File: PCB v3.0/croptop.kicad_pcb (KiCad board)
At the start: 4 copper layers, 190.1 x 122.2 mm, 273 parts, among them J1 TSM-106-01-L-SV, J10 1702474, J11 1702474, J12 1702474, J13 1702474, J14 1702474, J15 TSM-112-01-L-DV, J16 DM3D-SF, J17 Conn_01x01, J18 Conn_01x01, J2 0473460001, J3 87583-2010BLF, J4 NREC004SABC-M30RC, J5 Conn_01x01, J6 Conn_01x01, J7 1702474, J8 1702474, J9 1702474, Q1 BSS138, Q2 BSS84, Q3 Q2319ADS-T1-GE3, Q4 BSS138, Q5 BSS138, Q6 BSS138, SW1 SW_Push, SW2 SW_Push, SW3 SW_Push, SW4 SW_Push, U1 PIC32MX795F512L, U18 74HCT125D653, U19 AP22802AW5, U2 REG71055DDC, U20 AD7799, U21 AP22802AW5, U22 TPD4E1U06DBV, U23 AP22802AW5, U24 TPD4E1U06DBV, U25 TPD4E1U06DBV, U26 TPD4E1U06DBV, U27 DRV8872, U28 DRV8825, U29 AP22802AW5, U3 AP22802AW5, U30 TPD4E1U06DBV, U31 TPD4E1U06DBV, U32 AP22802AW5, U33 AP22802AW5, U34 TPD4E1U06DBV, U35 TPD4E1U06DBV, U36 AP22802AW5, U37 TPD4E1U06DBV, U38 TPD4E1U06DBV, U39 LIS3DSHTR, U40 CAM-M8C-0, U41 Si7006-A20, U5 TPS62131RGT, U6 TPS70950DBV, U7 TPD4E1U06DBV, U8 TPD4E1U06DBV, Y1 ABLS-8.000MHZ-B4-T, Y3 ABS07-32.768KHZ-1-T

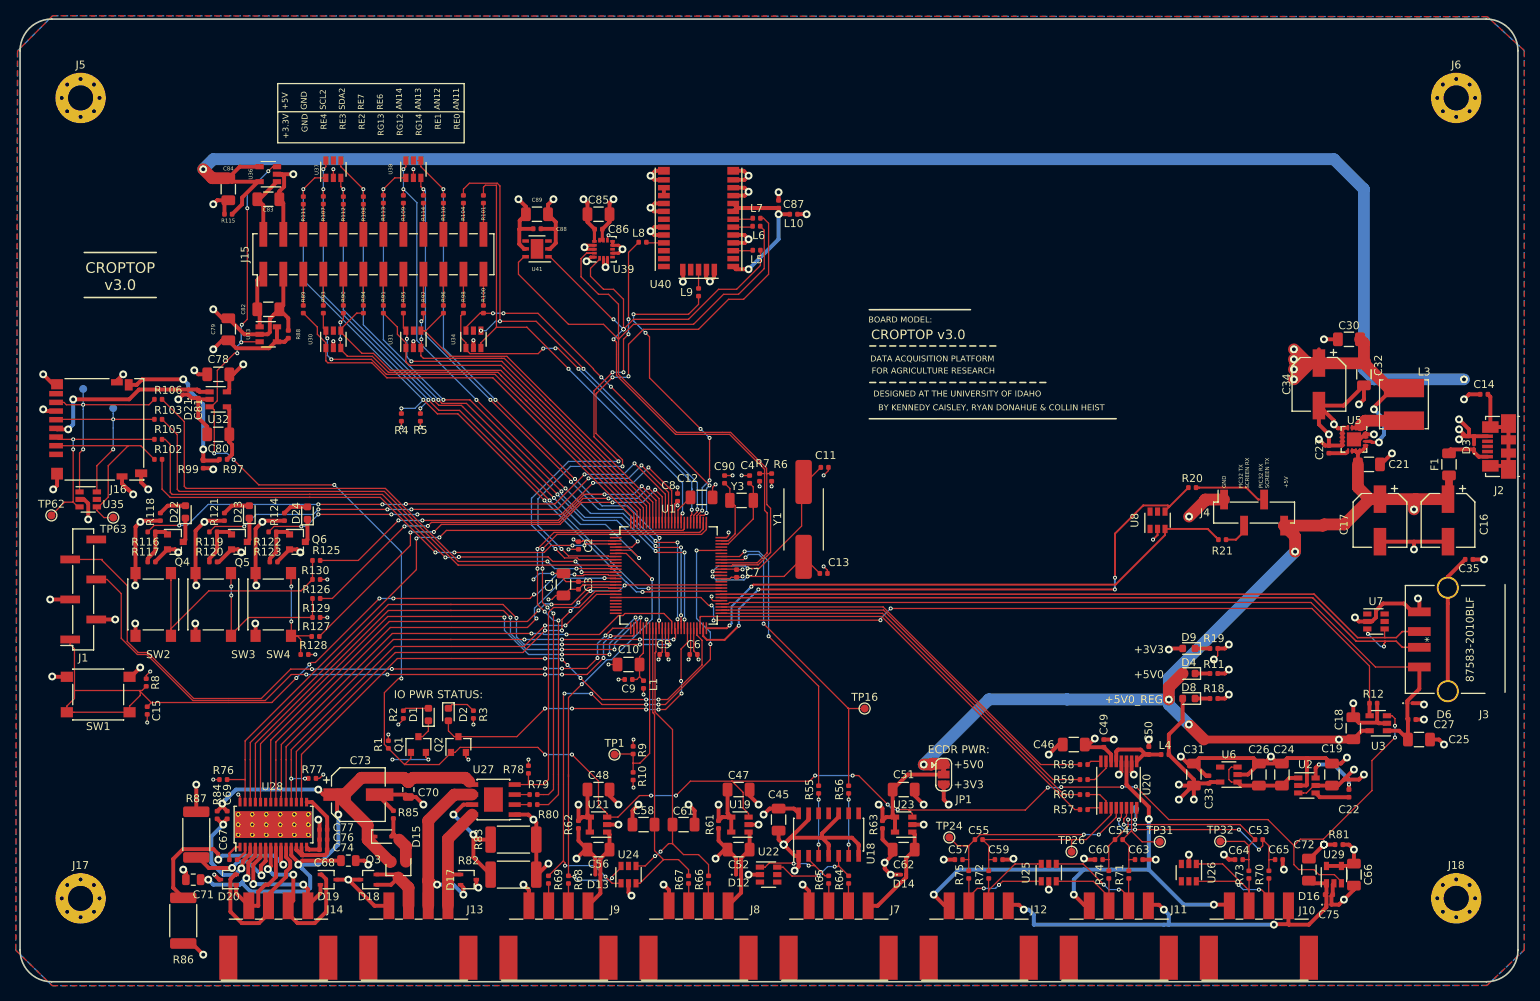
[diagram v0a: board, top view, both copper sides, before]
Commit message: Updated readme, added graphics to PCBv3
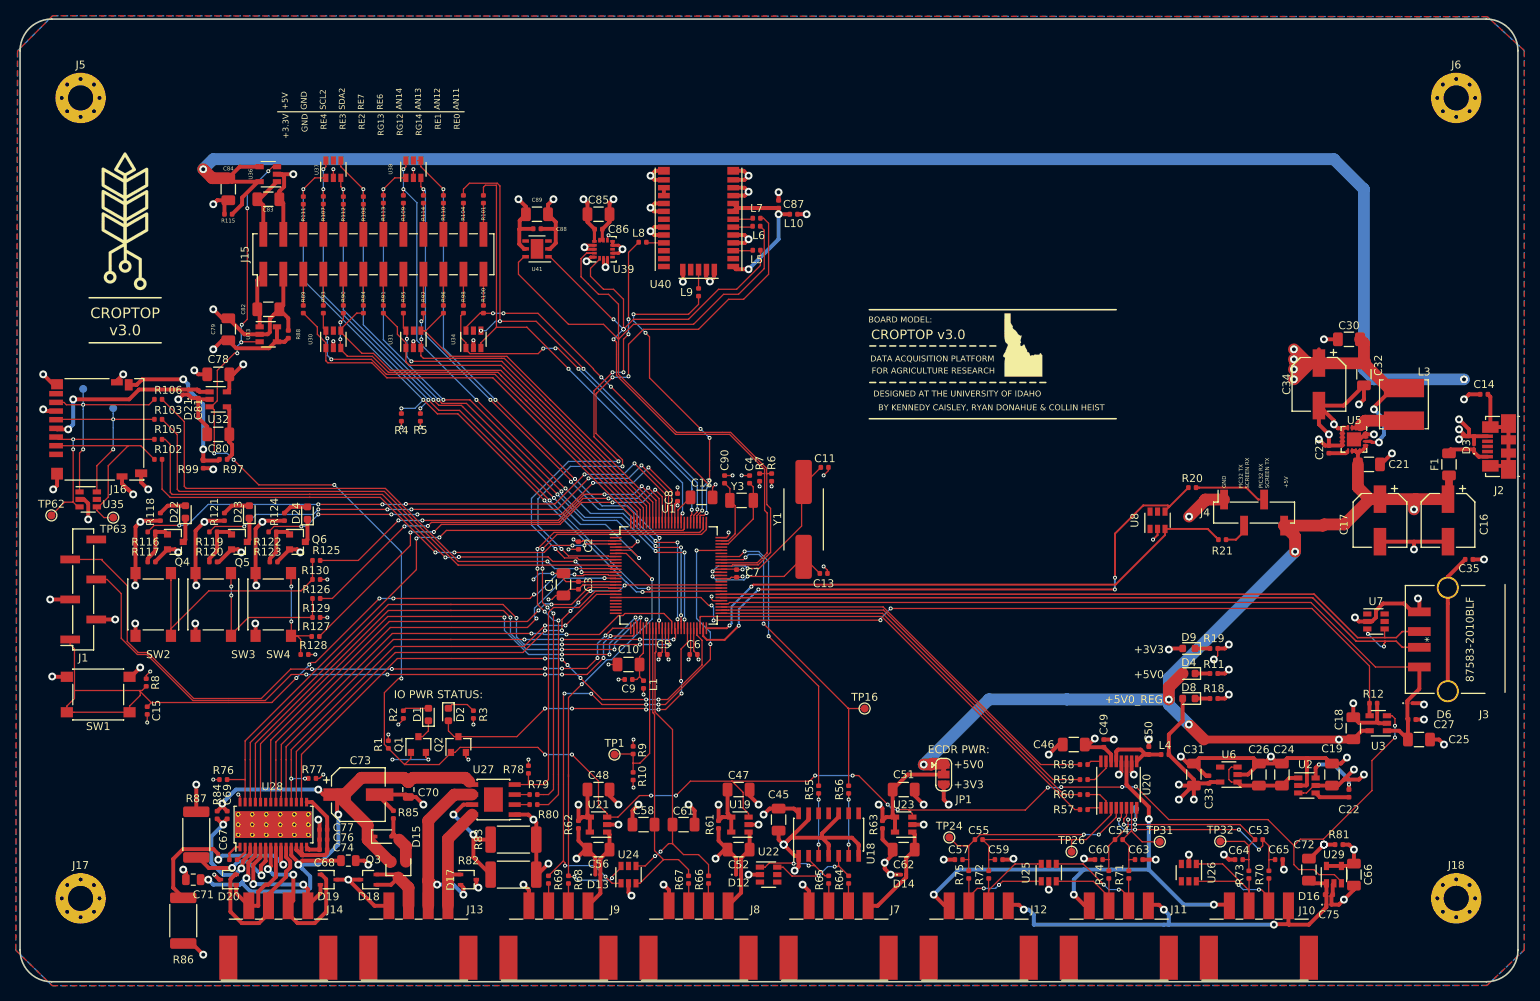
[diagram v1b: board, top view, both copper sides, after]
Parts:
- added  : , croptop:idaho, F.Cu at (179.6, 81.4)
- added G***: LOGO, croptop:croptoplogo, F.Cu at (65.5, 66.4)
